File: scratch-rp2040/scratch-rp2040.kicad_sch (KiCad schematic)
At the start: 26 parts, among them P1 USB_C_Plug_USB2.0, SW1 SW_SPST, U1 RP2040, U2 NCP1117-3.3_SOT223, U3 W25Q128JVS, Y1 Crystal_Small

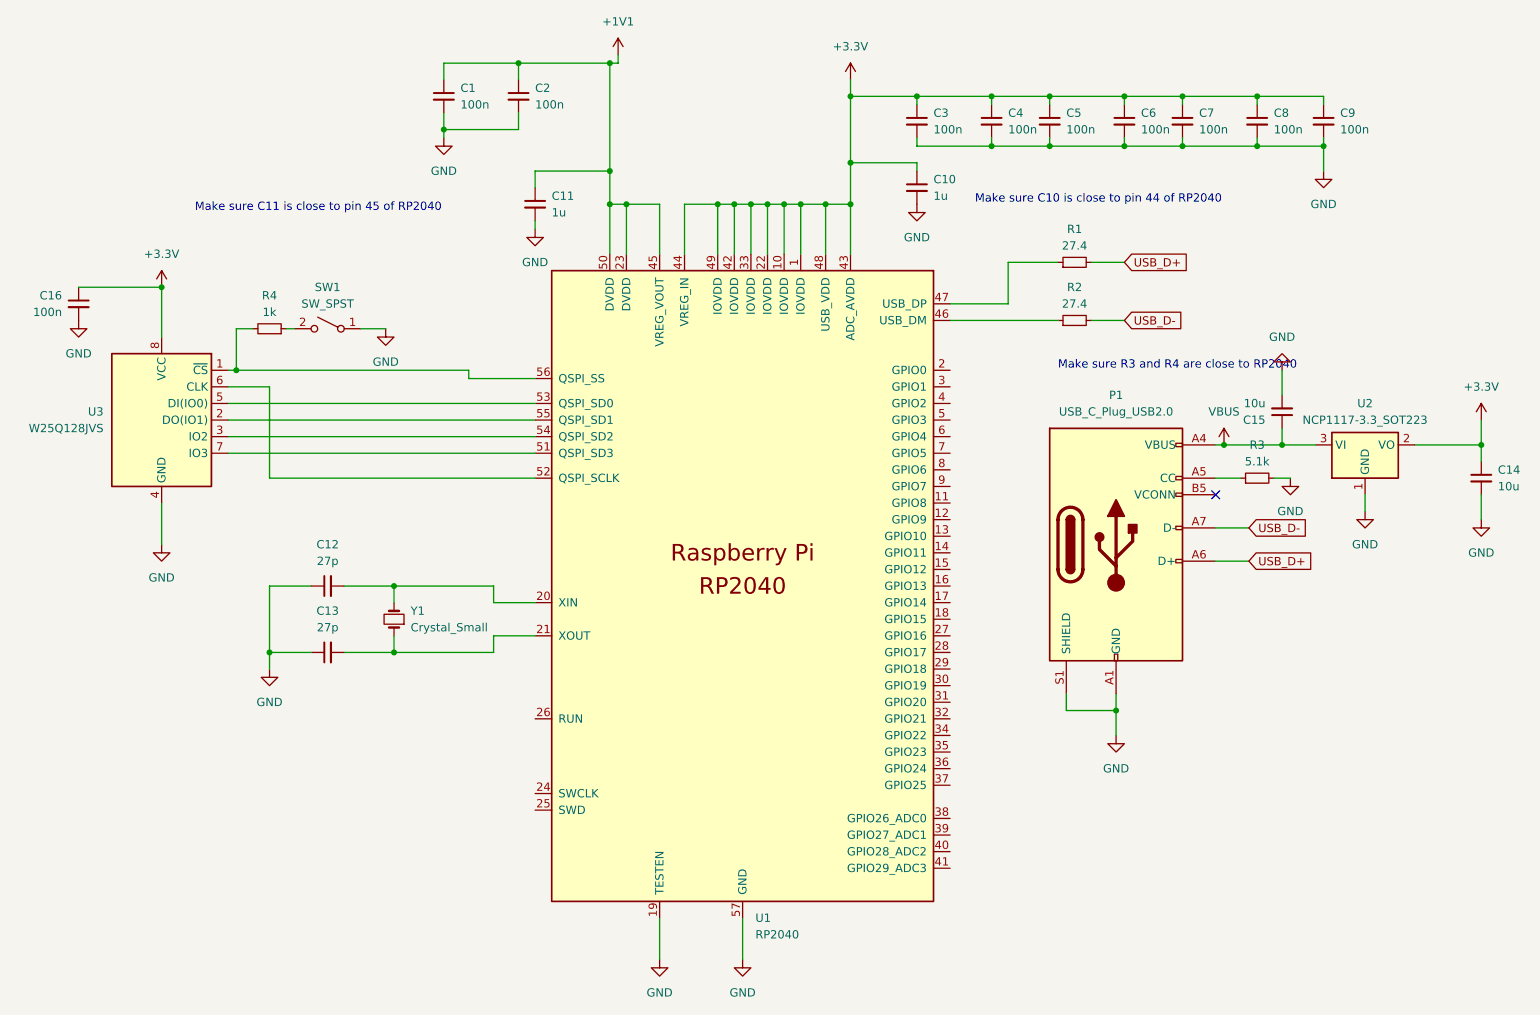
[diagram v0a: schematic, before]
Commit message: footprint assigned
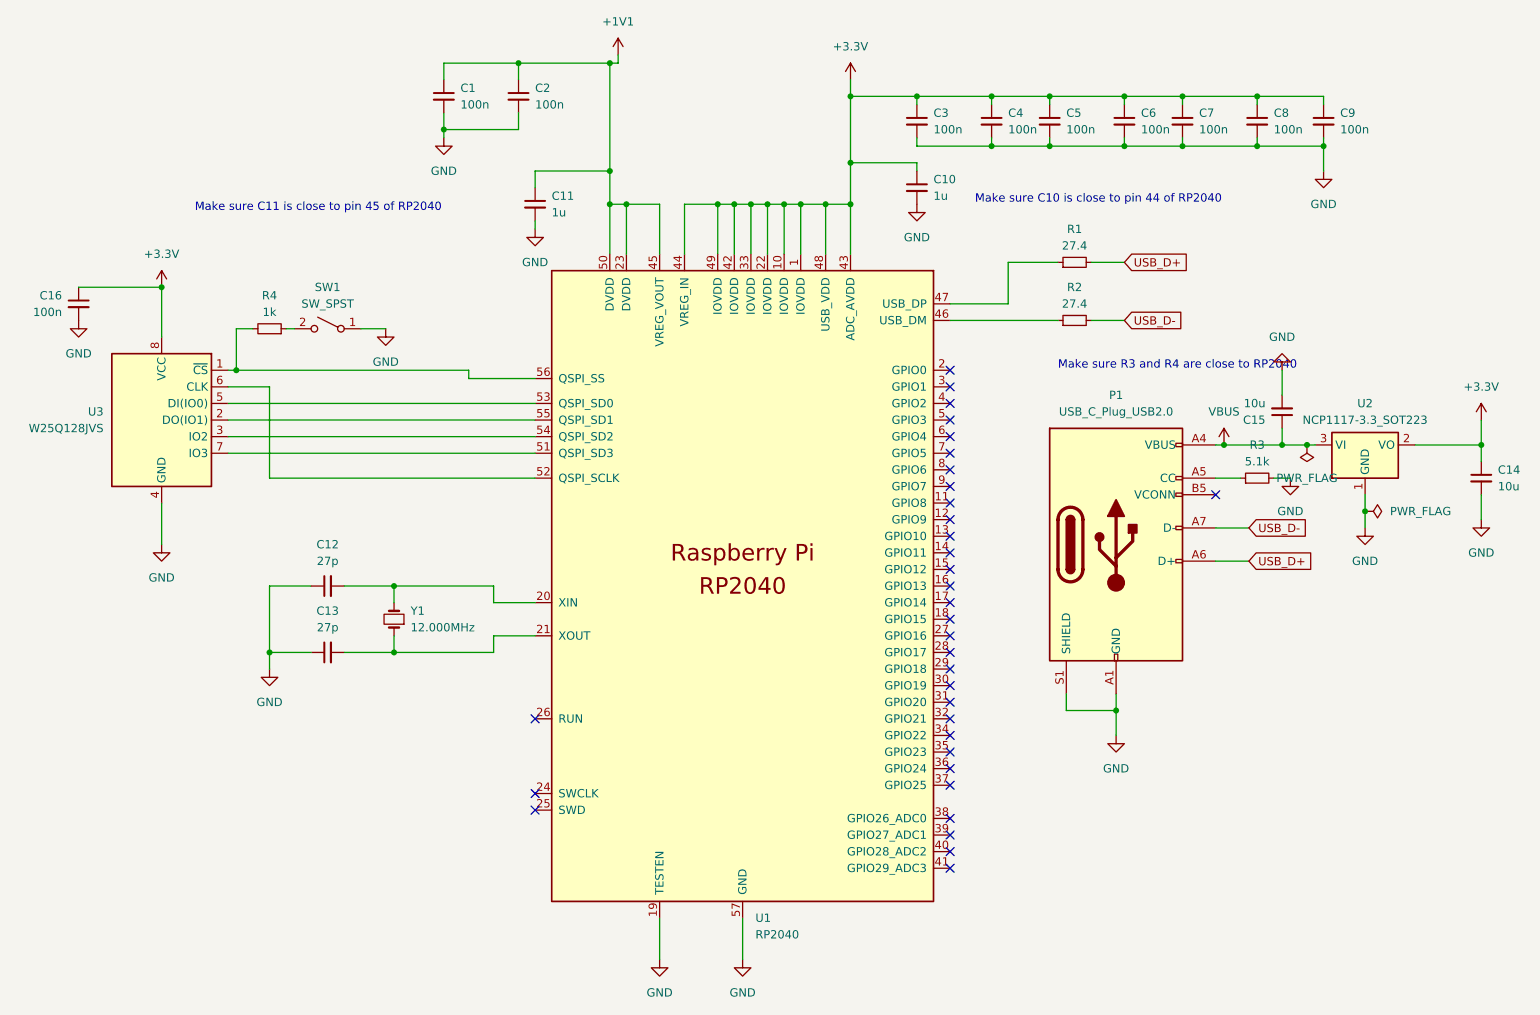
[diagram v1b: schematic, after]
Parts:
- C1, C10, C11, C12, C13, C16, C2, C3, C4, C5, C6, C7, C8, C9: footprint (none) -> Capacitor_SMD:C_0402_1005Metric
- C14, C15: footprint (none) -> Capacitor_SMD:C_0805_2012Metric
- P1: footprint (none) -> Connector_USB:USB_C_Receptacle_GCT_USB4135-GF-A_6P_TopMnt_Horizontal
- R1, R2, R3, R4: footprint (none) -> Resistor_SMD:R_0402_1005Metric
- SW1: footprint (none) -> Button_Switch_SMD:SW_DIP_SPSTx01_Slide_6.7x4.1mm_W6.73mm_P2.54mm_LowProfile_JPin
- U1: footprint RP2040_minimal:RP2040-QFN-56 -> Package_DFN_QFN:QFN-56-1EP_7x7mm_P0.4mm_EP3.2x3.2mm
- Y1: value Crystal_Small -> 12.000MHz; footprint (none) -> Crystal:Crystal_SMD_3225-4Pin_3.2x2.5mm
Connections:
- no-connect marks 1 -> 34

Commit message: categorized footprints
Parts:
- P1: footprint Connector_USB:USB_C_Receptacle_GCT_USB4135-GF-A_6P_TopMnt_Horizontal -> Connector_USB:USB_C_Receptacle_GCT_USB4105-xx-A_16P_TopMnt_Horizontal
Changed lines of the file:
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@@
       (effects (font (size 1.27 1.27)))
     )
-    (property "Footprint" "Connector_USB:USB_C_Receptacle_GCT_USB4135-GF-A_6P_TopMnt_Horizontal" (at 214.63 97.79 0)
+    (property "Footprint" "Connector_USB:USB_C_Receptacle_GCT_USB4105-xx-A_16P_TopMnt_Horizontal" (at 214.63 97.79 0)
       (effects (font (size 1.27 1.27)) hide)
     )

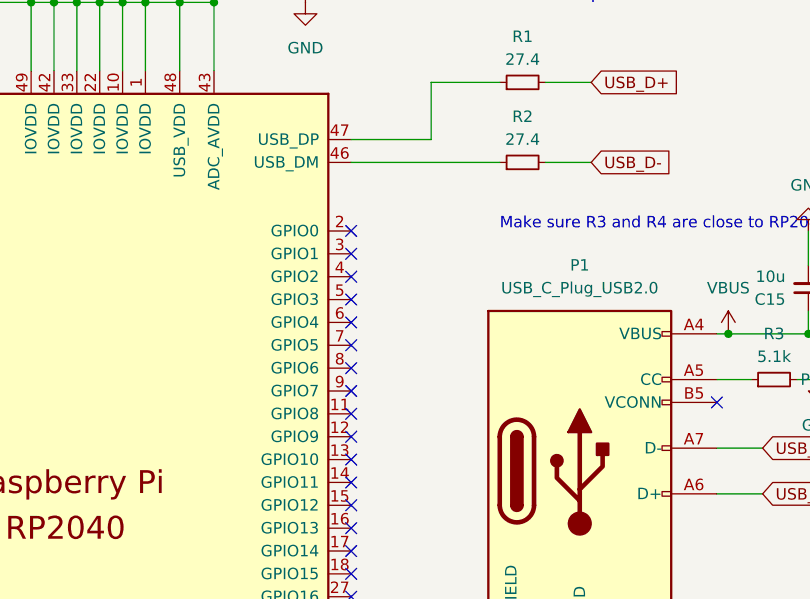
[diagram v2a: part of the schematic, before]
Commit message: pcb wiring including switches
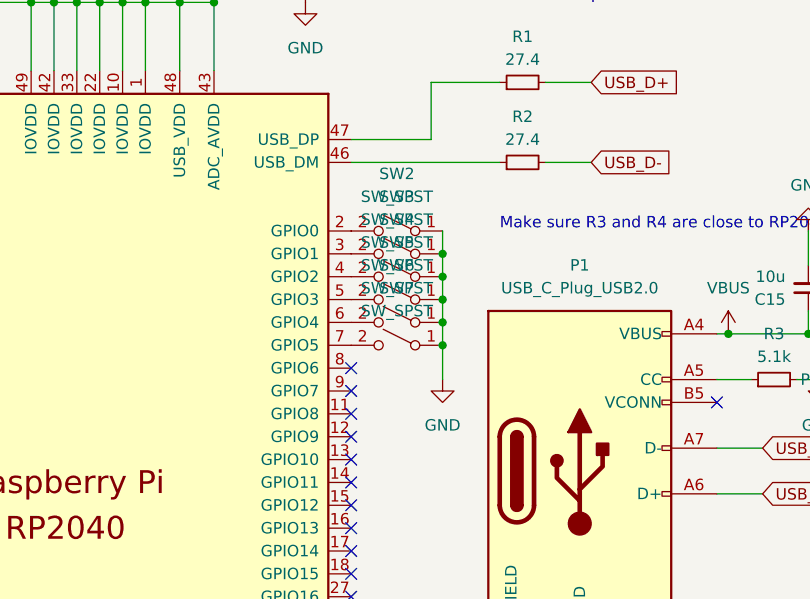
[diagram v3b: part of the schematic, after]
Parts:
- added SW2, SW3, SW4, SW5, SW6, SW7: SW_SPST, Button_Switch_SMD:SW_SPST_B3U-1000P, symbol Switch:SW_SPST
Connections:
- net GND: now also SW2.1 (A), SW3.1 (A), SW4.1 (A), SW5.1 (A), SW6.1 (A), SW7.1 (A)
- net at U1.2 (GPIO0): now also SW2.2 (B)
- net at U1.3 (GPIO1): now also SW3.2 (B)
- net at U1.4 (GPIO2): now also SW4.2 (B)
- net at U1.5 (GPIO3): now also SW5.2 (B)
- net at U1.6 (GPIO4): now also SW6.2 (B)
- net at U1.7 (GPIO5): now also SW7.2 (B)
- no-connect marks 34 -> 28
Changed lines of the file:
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@@
   (junction (at 154.94 45.72) (diameter 0) (color 0 0 0 0)
   )
+  (junction (at 195.58 73.66) (diameter 0) (color 0 0 0 0)
+  )
   (junction (at 170.18 45.72) (diameter 0) (color 0 0 0 0)
   )
@@
   (junction (at 170.18 39.37) (diameter 0) (color 0 0 0 0)
   )
+  (junction (at 195.58 81.28) (diameter 0) (color 0 0 0 0)
+  )
   (junction (at 166.37 45.72) (diameter 0) (color 0 0 0 0)
   )
+  (junction (at 195.58 78.74) (diameter 0) (color 0 0 0 0)
+  )
   (junction (at 191.77 29.21) (diameter 0) (color 0 0 0 0)
   )
+  (junction (at 195.58 76.2) (diameter 0) (color 0 0 0 0)
+  )
   (junction (at 81.28 114.3) (diameter 0) (color 0 0 0 0)
+  )
+  (junction (at 195.58 83.82) (diameter 0) (color 0 0 0 0)
   )
   (junction (at 100.33 104.14) (diameter 0) (color 0 0 0 0)
@@
   (no_connect (at 121.92 138.43))
   (no_connect (at 185.42 144.78))
-  (no_connect (at 185.42 71.12))
   (no_connect (at 226.06 90.17))
   (no_connect (at 185.42 86.36))
   (no_connect (at 185.42 106.68))
-  (no_connect (at 185.42 76.2))
   (no_connect (at 185.42 111.76))
   (no_connect (at 185.42 99.06))
-  (no_connect (at 185.42 78.74))
   (no_connect (at 185.42 116.84))
   (no_connect (at 185.42 91.44))
@@
   (no_connect (at 185.42 93.98))
   (no_connect (at 185.42 139.7))
-  (no_connect (at 185.42 73.66))
   (no_connect (at 185.42 121.92))
   (no_connect (at 185.42 124.46))
-  (no_connect (at 185.42 81.28))
   (no_connect (at 185.42 101.6))
   (no_connect (at 185.42 96.52))
   (no_connect (at 121.92 135.89))
-  (no_connect (at 185.42 83.82))
   (no_connect (at 185.42 88.9))
   (no_connect (at 185.42 132.08))
@@
     (stroke (width 0) (type default))
   )
+  (wire (pts (xy 195.58 81.28) (xy 195.58 83.82))
+    (stroke (width 0) (type default))
+  )
   (wire (pts (xy 115.57 106.68) (xy 121.92 106.68))
     (stroke (width 0) (type default))
@@
     (stroke (width 0) (type default))
   )
+  (wire (pts (xy 195.58 71.12) (xy 195.58 73.66))
+    (stroke (width 0) (type default))
+  )
   (wire (pts (xy 100.33 114.3) (xy 115.57 114.3))
     (stroke (width 0) (type default))
@@
     (stroke (width 0) (type default))
   )
+  (wire (pts (xy 195.58 76.2) (xy 195.58 78.74))
+    (stroke (width 0) (type default))
+  )
   (wire (pts (xy 185.42 60.96) (xy 194.31 60.96))
     (stroke (width 0) (type default))
@@
     (stroke (width 0) (type default))
   )
+  (wire (pts (xy 195.58 83.82) (xy 195.58 87.63))
+    (stroke (width 0) (type default))
+  )
   (wire (pts (xy 248.92 92.71) (xy 248.92 95.25))
     (stroke (width 0) (type default))
@@
     (stroke (width 0) (type default))
   )
+  (wire (pts (xy 195.58 78.74) (xy 195.58 81.28))
+    (stroke (width 0) (type default))
+  )
   (wire (pts (xy 236.22 82.55) (xy 236.22 80.01))
     (stroke (width 0) (type default))
@@
   )
   (wire (pts (xy 119.38 24.13) (xy 133.35 24.13))
+    (stroke (width 0) (type default))
+  )
+  (wire (pts (xy 195.58 73.66) (xy 195.58 76.2))
     (stroke (width 0) (type default))
   )
@@
     )
   )
+  (symbol (lib_id "power:GND") (at 195.58 87.63 0) (unit 1)
+    (in_bom yes) (on_board yes) (dnp no) (fields_autoplaced)
+    (property "Reference" "#PWR021" (at 195.58 93.98 0)
+      (effects (font (size 1.27 1.27)) hide)
+    )
+    (property "Value" "GND" (at 195.58 92.71 0)
+      (effects (font (size 1.27 1.27)))
+    )
+    (property "Footprint" "" (at 195.58 87.63 0)
+      (effects (font (size 1.27 1.27)) hide)
+    )
+    (property "Datasheet" "" (at 195.58 87.63 0)
+      (effects (font (size 1.27 1.27)) hide)
+    )
+    (pin "1")
+    (instances
+      (project "scratch-rp2040"
+        (path "/02689c9b-b226-4021-8c02-6978486ff0a8"
+          (reference "#PWR021") (unit 1)
+        )
+      )
+    )
+  )
   (symbol (lib_id "Device:C_Small") (at 191.77 33.02 0) (unit 1)
     (in_bom yes) (on_board yes) (dnp no) (fields_autoplaced)
@@
         (path "/02689c9b-b226-4021-8c02-6978486ff0a8"
           (reference "#PWR07") (unit 1)
+        )
+      )
+    )
+  )
+  (symbol (lib_id "Switch:SW_SPST") (at 190.5 81.28 0) (mirror y) (unit 1)
+    (in_bom yes) (on_board yes) (dnp no) (fields_autoplaced)
+    (property "Reference" "SW6" (at 190.5 74.93 0)
+      (effects (font (size 1.27 1.27)))
+    )
+    (property "Value" "SW_SPST" (at 190.5 77.47 0)
+      (effects (font (size 1.27 1.27)))
+    )
+    (property "Footprint" "Button_Switch_SMD:SW_SPST_B3U-1000P" (at 190.5 81.28 0)
+      (effects (font (size 1.27 1.27)) hide)
+    )
+    (property "Datasheet" "~" (at 190.5 81.28 0)
+      (effects (font (size 1.27 1.27)) hide)
+    )
+    (pin "1")
+    (pin "2")
+    (instances
+      (project "scratch-rp2040"
+        (path "/02689c9b-b226-4021-8c02-6978486ff0a8"
+          (reference "SW6") (unit 1)
         )
       )
@@
     )
   )
+  (symbol (lib_id "Switch:SW_SPST") (at 190.5 71.12 0) (mirror y) (unit 1)
+    (in_bom yes) (on_board yes) (dnp no) (fields_autoplaced)
+    (property "Reference" "SW2" (at 190.5 64.77 0)
+      (effects (font (size 1.27 1.27)))
+    )
+    (property "Value" "SW_SPST" (at 190.5 67.31 0)
+      (effects (font (size 1.27 1.27)))
+    )
+    (property "Footprint" "Button_Switch_SMD:SW_SPST_B3U-1000P" (at 190.5 71.12 0)
+      (effects (font (size 1.27 1.27)) hide)
+    )
+    (property "Datasheet" "~" (at 190.5 71.12 0)
+      (effects (font (size 1.27 1.27)) hide)
+    )
+    (pin "1")
+    (pin "2")
+    (instances
+      (project "scratch-rp2040"
+        (path "/02689c9b-b226-4021-8c02-6978486ff0a8"
+          (reference "SW2") (unit 1)
+        )
+      )
+    )
+  )
   (symbol (lib_id "Device:Crystal_Small") (at 100.33 109.22 90) (unit 1)
     (in_bom yes) (on_board yes) (dnp no) (fields_autoplaced)
@@
     )
   )
+  (symbol (lib_id "Switch:SW_SPST") (at 190.5 78.74 0) (mirror y) (unit 1)
+    (in_bom yes) (on_board yes) (dnp no) (fields_autoplaced)
+    (property "Reference" "SW5" (at 190.5 72.39 0)
+      (effects (font (size 1.27 1.27)))
+    )
+    (property "Value" "SW_SPST" (at 190.5 74.93 0)
+      (effects (font (size 1.27 1.27)))
+    )
+    (property "Footprint" "Button_Switch_SMD:SW_SPST_B3U-1000P" (at 190.5 78.74 0)
+      (effects (font (size 1.27 1.27)) hide)
+    )
+    (property "Datasheet" "~" (at 190.5 78.74 0)
+      (effects (font (size 1.27 1.27)) hide)
+    )
+    (pin "1")
+    (pin "2")
+    (instances
+      (project "scratch-rp2040"
+        (path "/02689c9b-b226-4021-8c02-6978486ff0a8"
+          (reference "SW5") (unit 1)
+        )
+      )
+    )
+  )
   (symbol (lib_id "Device:C_Small") (at 107.95 29.21 0) (unit 1)
     (in_bom yes) (on_board yes) (dnp no) (fields_autoplaced)
@@
     )
   )
+  (symbol (lib_id "Switch:SW_SPST") (at 190.5 73.66 0) (mirror y) (unit 1)
+    (in_bom yes) (on_board yes) (dnp no) (fields_autoplaced)
+    (property "Reference" "SW3" (at 190.5 67.31 0)
+      (effects (font (size 1.27 1.27)))
+    )
+    (property "Value" "SW_SPST" (at 190.5 69.85 0)
+      (effects (font (size 1.27 1.27)))
+    )
+    (property "Footprint" "Button_Switch_SMD:SW_SPST_B3U-1000P" (at 190.5 73.66 0)
+      (effects (font (size 1.27 1.27)) hide)
+    )
+    (property "Datasheet" "~" (at 190.5 73.66 0)
+      (effects (font (size 1.27 1.27)) hide)
+    )
+    (pin "1")
+    (pin "2")
+    (instances
+      (project "scratch-rp2040"
+        (path "/02689c9b-b226-4021-8c02-6978486ff0a8"
+          (reference "SW3") (unit 1)
+        )
+      )
+    )
+  )
   (symbol (lib_id "power:GND") (at 237.49 87.63 0) (unit 1)
     (in_bom yes) (on_board yes) (dnp no) (fields_autoplaced)
@@
         (path "/02689c9b-b226-4021-8c02-6978486ff0a8"
           (reference "#PWR03") (unit 1)
+        )
+      )
+    )
+  )
+  (symbol (lib_id "Switch:SW_SPST") (at 190.5 83.82 0) (mirror y) (unit 1)
+    (in_bom yes) (on_board yes) (dnp no) (fields_autoplaced)
+    (property "Reference" "SW7" (at 190.5 77.47 0)
+      (effects (font (size 1.27 1.27)))
+    )
+    (property "Value" "SW_SPST" (at 190.5 80.01 0)
+      (effects (font (size 1.27 1.27)))
+    )
+    (property "Footprint" "Button_Switch_SMD:SW_SPST_B3U-1000P" (at 190.5 83.82 0)
+      (effects (font (size 1.27 1.27)) hide)
+    )
+    (property "Datasheet" "~" (at 190.5 83.82 0)
+      (effects (font (size 1.27 1.27)) hide)
+    )
+    (pin "1")
+    (pin "2")
+    (instances
+      (project "scratch-rp2040"
+        (path "/02689c9b-b226-4021-8c02-6978486ff0a8"
+          (reference "SW7") (unit 1)
         )
       )
@@
         )
       )
+    )
+  )
+  (symbol (lib_id "Switch:SW_SPST") (at 190.5 76.2 0) (mirror y) (unit 1)
+    (in_bom yes) (on_board yes) (dnp no) (fields_autoplaced)
+    (property "Reference" "SW4" (at 190.5 69.85 0)
+      (effects (font (size 1.27 1.27)))
+    )
+    (property "Value" "SW_SPST" (at 190.5 72.39 0)
+      (effects (font (size 1.27 1.27)))
+    )
+    (property "Footprint" "Button_Switch_SMD:SW_SPST_B3U-1000P" (at 190.5 76.2 0)
+      (effects (font (size 1.27 1.27)) hide)
+    )
+    (property "Datasheet" "~" (at 190.5 76.2 0)
+      (effects (font (size 1.27 1.27)) hide)
+    )
+    (pin "1")
+    (pin "2")
+    (instances
+      (project "scratch-rp2040"
+        (path "/02689c9b-b226-4021-8c02-6978486ff0a8"
+          (reference "SW4") (unit 1)
+        )
+      )

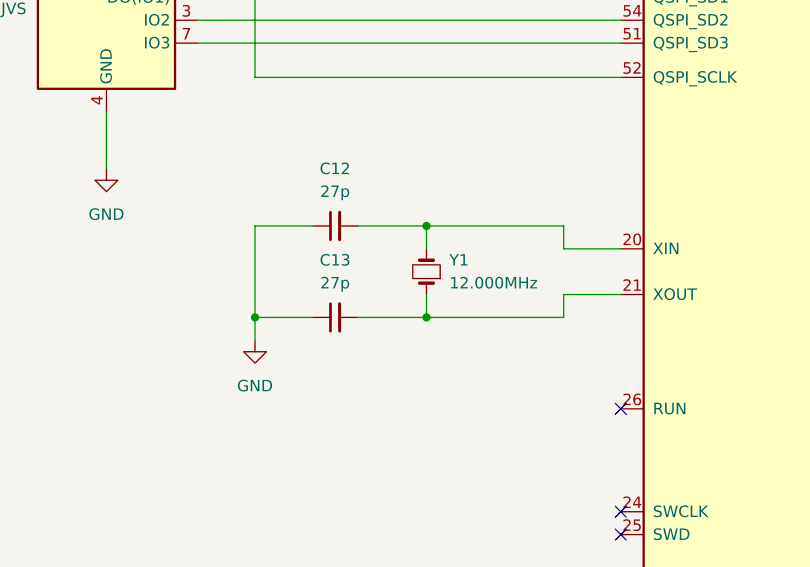
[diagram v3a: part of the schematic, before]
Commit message: footprint updated, looking jlcpcb assembly parts lib
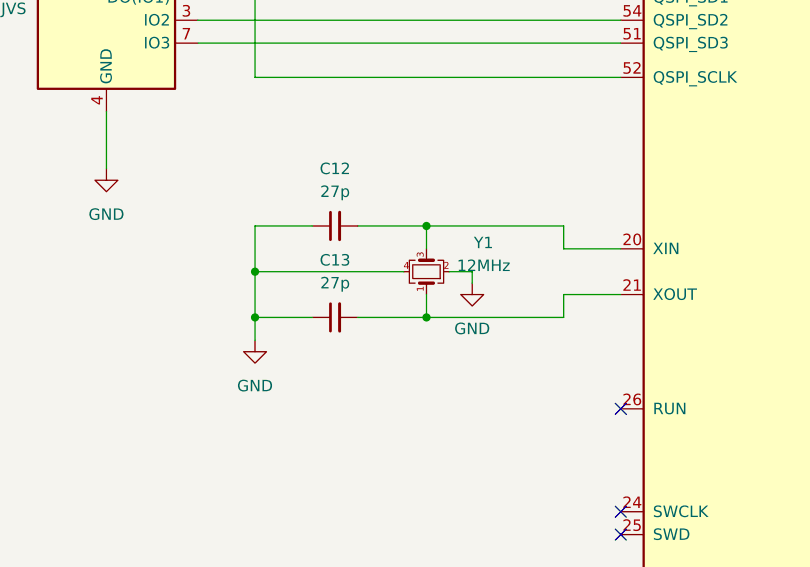
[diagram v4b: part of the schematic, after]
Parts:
- removed Y1: 12.000MHz, Crystal:Crystal_SMD_3225-4Pin_3.2x2.5mm, symbol Device:Crystal_Small
- added Y1: 12MHz, Crystal:Crystal_SMD_3225-4Pin_3.2x2.5mm, symbol Device:Crystal_GND24_Small
- C1, C10, C11, C12, C13, C16, C2, C3, C4, C5, C6, C7, C8, C9: footprint Capacitor_SMD:C_0402_1005Metric -> Capacitor_SMD:C_0201_0603Metric
- C14, C15: footprint Capacitor_SMD:C_0805_2012Metric -> Capacitor_SMD:C_0402_1005Metric
- P1: footprint Connector_USB:USB_C_Receptacle_GCT_USB4105-xx-A_16P_TopMnt_Horizontal -> Connector_USB:USB_C_Receptacle_GCT_USB4135-GF-A_6P_TopMnt_Horizontal
- R1, R2, R3, R4: footprint Resistor_SMD:R_0402_1005Metric -> Resistor_SMD:R_0201_0603Metric
- SW1: footprint Button_Switch_SMD:SW_DIP_SPSTx01_Slide_6.7x4.1mm_W6.73mm_P2.54mm_LowProfile_JPin -> Button_Switch_SMD:SW_SPDT_PCM12
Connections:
- net GND: now also Y1.2, Y1.4
- net at C12.2, U1.20 (XIN): now also Y1.3
- net at C13.2, U1.21 (XOUT): now also Y1.1
